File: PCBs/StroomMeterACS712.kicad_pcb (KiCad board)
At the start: 2 copper layers, 13 parts, among them J1 OLED1604, J2 ACS712, J3 PWR_5V_pin, J4 WS2812, J5 PWR_5V_jst, Q1 BC547, Q2 BC547, U1 WeMos_D1_mini

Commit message: WS2812 toegevoegd
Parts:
- moved J3 8.55 mm to (139.7, 45.1), turned to -90 degrees
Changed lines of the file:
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@@
   )
   (paper "A4")
+  (title_block
+    (title "ACS712 stroommeter")
+    (date "2022-12-20")
+    (rev "0.01")
+    (company "Easylab4kids.nl")
+  )
   (layers
     (0 "F.Cu" signal)
@@
   (net 16 "unconnected-(U1-Pad16)")
   (footprint "Connector_PinHeader_2.00mm:PinHeader_1x02_P2.00mm_Vertical_SMD_Pin1Right" (layer "F.Cu")
-    (at 131.15 45.1)
+    (at 139.7 45.1 -90)
     (descr "surface-mounted straight pin header, 1x02, 2.00mm pitch, single row, style 2 (pin 1 right)")
     (tags "Surface mounted pin header SMD 1x02 2.00mm single row style2 pin1 right")
@@
     (property "Sheetname" "")
     (attr smd)
-    (fp_text reference "J3" (at 0 -3.06) (layer "F.SilkS")
+    (fp_text reference "J3" (at 0 -3.06 90) (layer "F.SilkS")
       (effects (font (size 1 1) (thickness 0.15)))
     )
-    (fp_text value "PWR_5V_pin" (at 0 3.06) (layer "F.Fab")
+    (fp_text value "PWR_5V_pin" (at 0 3.06 90) (layer "F.Fab")
       (effects (font (size 1 1) (thickness 0.15)))
     )
-    (fp_text user "${REFERENCE}" (at 0 0 90) (layer "F.Fab")
+    (fp_text user "${REFERENCE}" (at 0 0) (layer "F.Fab")
       (effects (font (size 1 1) (thickness 0.15)))
     )
@@
     (fp_line (start 1 2) (end -1 2) (layer "F.Fab") (width 0.1))
     (fp_line (start -1 -2) (end 0.25 -2) (layer "F.Fab") (width 0.1))
-    (pad "1" smd rect locked (at 1.175 -1) (size 2.35 0.85) (layers "F.Cu" "F.Paste" "F.Mask")
+    (pad "1" smd rect locked (at 1.175 -1 270) (size 2.35 0.85) (layers "F.Cu" "F.Paste" "F.Mask")
       (net 3 "VCC") (pinfunction "Pin_1") (pintype "passive"))
-    (pad "2" smd rect locked (at -1.175 1) (size 2.35 0.85) (layers "F.Cu" "F.Paste" "F.Mask")
+    (pad "2" smd rect locked (at -1.175 1 270) (size 2.35 0.85) (layers "F.Cu" "F.Paste" "F.Mask")
       (net 4 "GND") (pinfunction "Pin_2") (pintype "passive"))
     (model "${KICAD6_3DMODEL_DIR}/Connector_PinHeader_2.00mm.3dshapes/PinHeader_1x02_P2.00mm_Vertical_SMD_Pin1Right.wrl"

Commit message: PCb toegeovegd
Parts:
- added SW1: btnAanUit, Button_Switch_THT:KSA_Tactile_SPST, F.Cu at (120.9, 62.0)
- H1, H2, H3, H4: footprint MountingHole:MountingHole_3.2mm_M3 -> MountingHole:MountingHole_2.7mm_M2.5_Pad
- J1: footprint Display:Adafruit_SSD1306 -> Connector_PinHeader_2.00mm:PinHeader_1x03_P2.00mm_Vertical
- R1: value R1k -> R100
- moved R1 56.0 mm to (115.3, 49.3), turned to 180 degrees
- moved H3 54.2 mm to (67.1, 24.9)
- moved Q1 54.2 mm to (81.3, 24.9)
- moved J5 52.0 mm to (94.5, 24.9), turned to 180 degrees
- moved Q2 43.8 mm to (96.0, 60.5), turned to 90 degrees
- moved J1 40.9 mm to (113.3, 35.6)
- moved H4 37.9 mm to (67.6, 59.4)
- moved H1 33.4 mm to (109.2, 24.4)
- moved J4 19.2 mm to (104.1, 55.9)
- moved U1 18.0 mm to (90.2, 30.2), turned to -90 degrees
- moved H2 16.6 mm to (136.1, 59.9)
- moved J3 14.5 mm to (134.6, 31.5), turned to 0 degrees
- moved J2 4.57 mm to (135.1, 50.8), turned to 180 degrees
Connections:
- Q2 pad 2: BTN1 -> Net-(R1-Pad2)
- Q2 pad 3: Net-(Q2-Pad3) -> GND
- R1 pad 1: Net-(Q2-Pad3) -> Net-(R1-Pad1)
- R1 pad 2: GND -> Net-(R1-Pad2)

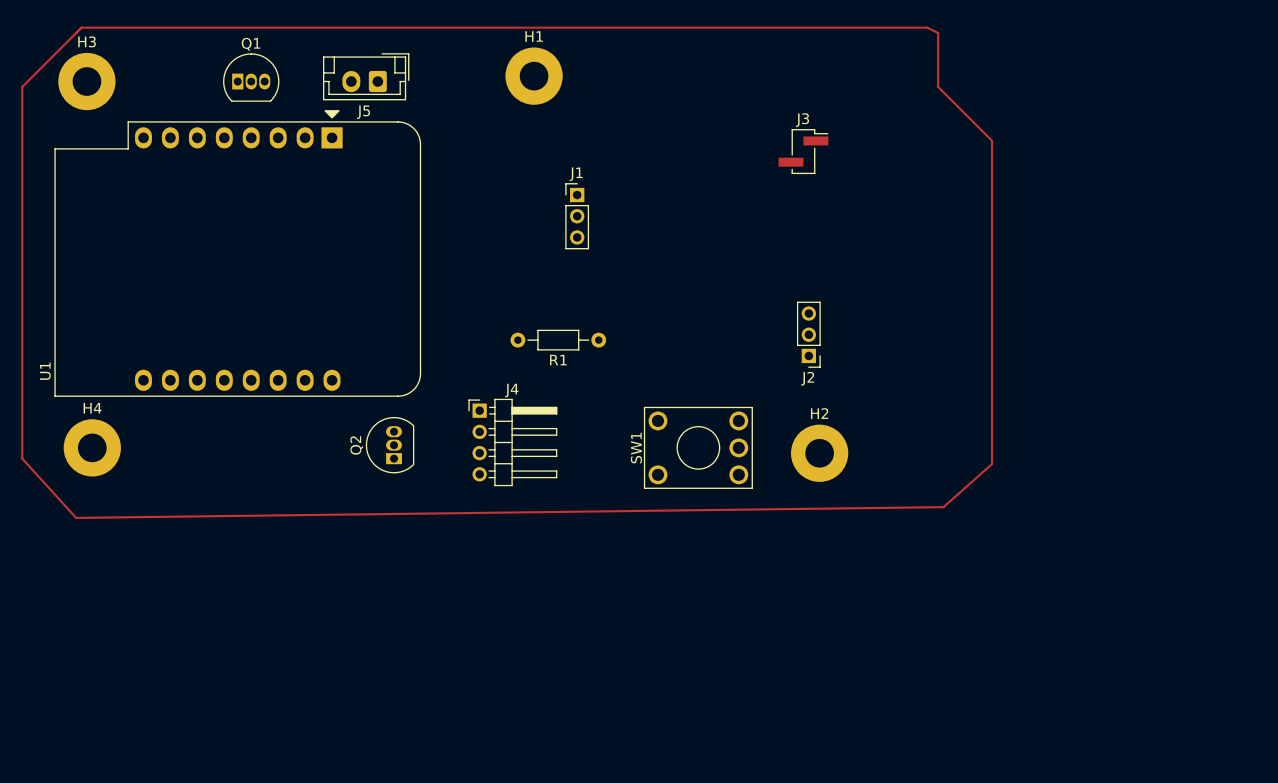
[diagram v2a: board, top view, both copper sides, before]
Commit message: PCF8574 toegevoegd aan PCB
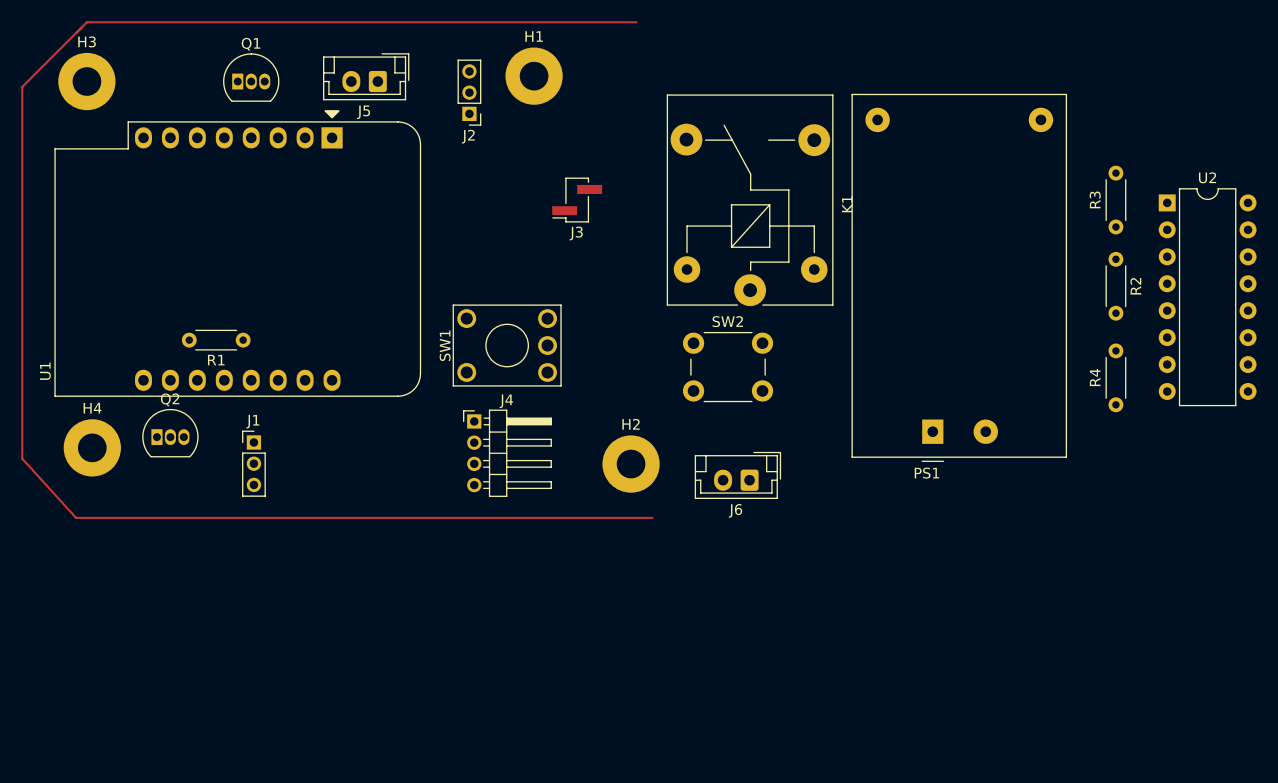
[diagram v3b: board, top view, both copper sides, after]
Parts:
- added J6: 230V_in, Connector_JST:JST_EH_B2B-EH-A_1x02_P2.50mm_Vertical, F.Cu at (129.5, 62.5)
- added K1: SRD-03VDC-SL-C_Relay, Relay_THT:Relay_SPDT_SANYOU_SRD_Series_Form_C, F.Cu at (129.6, 44.6)
- added PS1: HLK-PM01_220V, Converter_ACDC:Converter_ACDC_HiLink_HLK-PMxx, F.Cu at (146.8, 57.9)
- added R2: R10K, Resistor_THT:R_Axial_DIN0204_L3.6mm_D1.6mm_P5.08mm_Horizontal, F.Cu at (164.1, 41.7)
- added R3: R10K, Resistor_THT:R_Axial_DIN0204_L3.6mm_D1.6mm_P5.08mm_Horizontal, F.Cu at (164.1, 38.6)
- added R4: R10K, Resistor_THT:R_Axial_DIN0204_L3.6mm_D1.6mm_P5.08mm_Horizontal, F.Cu at (164.1, 55.4)
- added SW2: SW_SPDT, Button_Switch_THT:SW_PUSH_6mm, F.Cu at (124.3, 49.6)
- added U2: PCF8574A, Package_DIP:DIP-16_W7.62mm, F.Cu at (168.9, 36.3)
- R1: footprint Resistor_THT:R_Axial_DIN0204_L3.6mm_D1.6mm_P7.62mm_Horizontal -> Resistor_THT:R_Axial_DIN0204_L3.6mm_D1.6mm_P5.08mm_Horizontal
- moved J2 39.3 mm to (103.1, 27.9)
- moved J1 38.4 mm to (82.8, 58.9)
- moved R1 33.5 mm to (81.8, 49.3)
- moved Q2 22.4 mm to (73.7, 58.4), turned to 0 degrees
- moved J3 21.8 mm to (113.3, 36.1), turned to 180 degrees
- moved SW1 20.5 mm to (102.9, 52.3)
- moved H2 17.8 mm to (118.4, 61.0)
- moved J4 1.14 mm to (103.6, 56.9)
